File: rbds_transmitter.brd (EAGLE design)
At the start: 80 x 100 mm, 136 parts, among them J2 AVRISP-6, Q1 P-CH, Q2 P-Ch, Q3 P-Ch, T1 ATB3225-75032CT, T2 ATB3225-75032CT, U1 MAX2606, U2 TS974, U3 TS974, U4 MAX1551, U5 ATMEGA328, U6 TPS61030, U7 MCP4812, X1 16Mhz

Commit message: wiring up modules
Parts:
- moved ANT1 306.7 mm to (96.5, 119.4)
- moved C21 306.7 mm to (94.0, 114.3)
- moved C34 306.7 mm to (96.5, 114.3)
- moved C35 306.7 mm to (97.8, 101.0)
- moved C36 306.7 mm to (99.1, 105.4)
- moved C37 306.7 mm to (102.2, 105.4)
- moved L2 306.7 mm to (91.4, 105.4)
- moved R30 306.7 mm to (92.4, 110.5)
- moved R45 306.7 mm to (98.1, 110.5)
- moved TP8 306.7 mm to (92.7, 100.3)
- moved U1 306.7 mm to (95.2, 105.4)
- moved P1 302.8 mm to (129.5, 38.1), turned to 90 degrees
- moved B1 270.3 mm to (27.9, 21.6)
- moved J1 270.3 mm to (7.62, 21.6)
- moved L1 270.3 mm to (21.6, 38.1)
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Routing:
- net LCD5: track 0.00 -> 86.2 mm, vias 0 -> 2
- net LCD3: track 0.00 -> 84.2 mm, vias 0 -> 2
- net LCD2: track 0.00 -> 82.9 mm, vias 0 -> 2
- net LCD4: track 0.00 -> 80.5 mm
- net BPSK: track 5.10 -> 79.1 mm, vias 0 -> 1
- net LCD1: track 0.00 -> 63.4 mm, vias 0 -> 1
- net LCD0: track 0.00 -> 60.9 mm
- net AGND: track 36.7 -> 66.2 mm, vias 0 -> 2
- net CARRIER: track 0.00 -> 15.1 mm
- net ISP-MOSI: track 12.3 -> 0.00 mm
- net N$50: track 29.8 -> 20.7 mm
- net ISP-SCK: track 3.66 -> 12.7 mm
- net N$21: track 4.70 -> 7.50 mm
- net MOSI: track 0.00 -> 2.72 mm
- net SCK: track 0.00 -> 2.46 mm
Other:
- board size 80 x 100 mm -> 119.4 x 106.3 mm

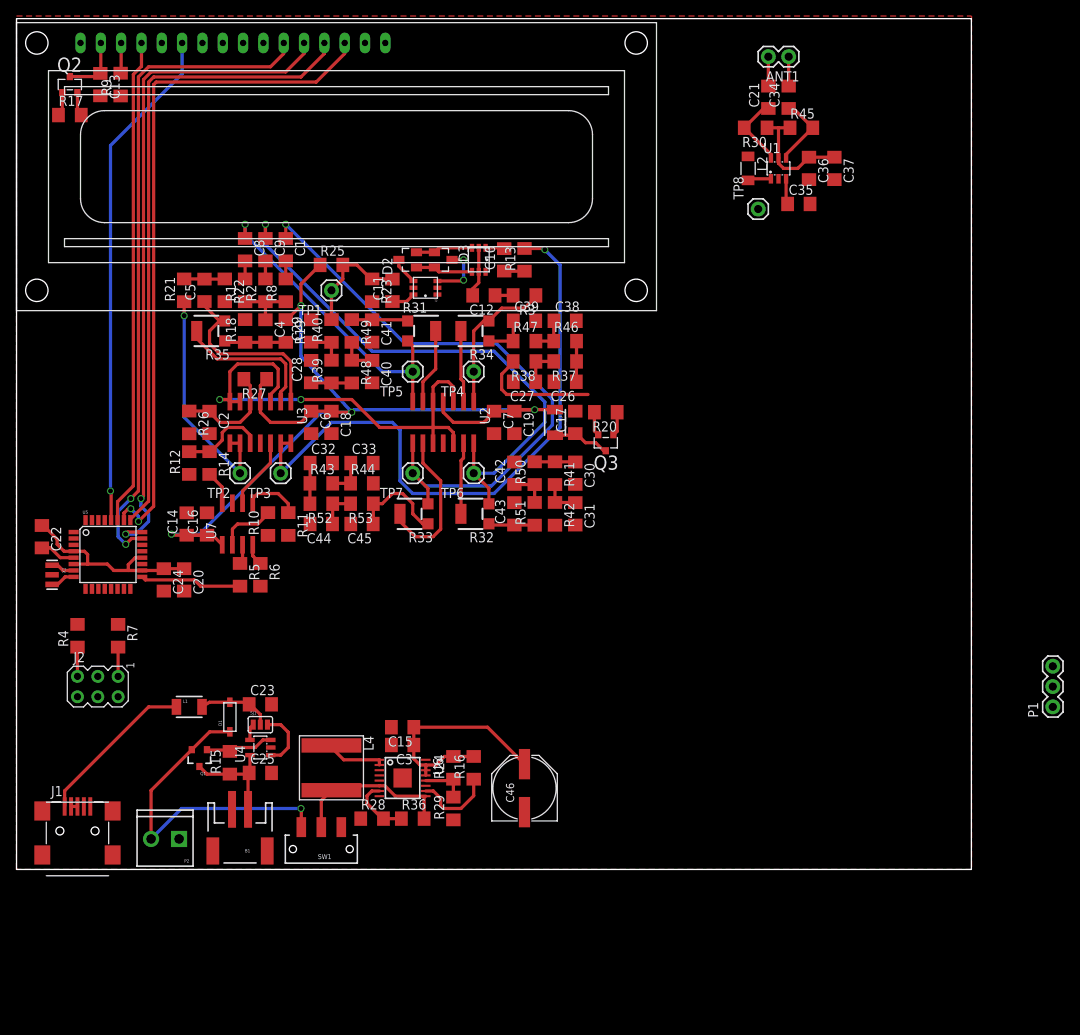
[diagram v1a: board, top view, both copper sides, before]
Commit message: changed mcu agnd to gnd: request engineering change form
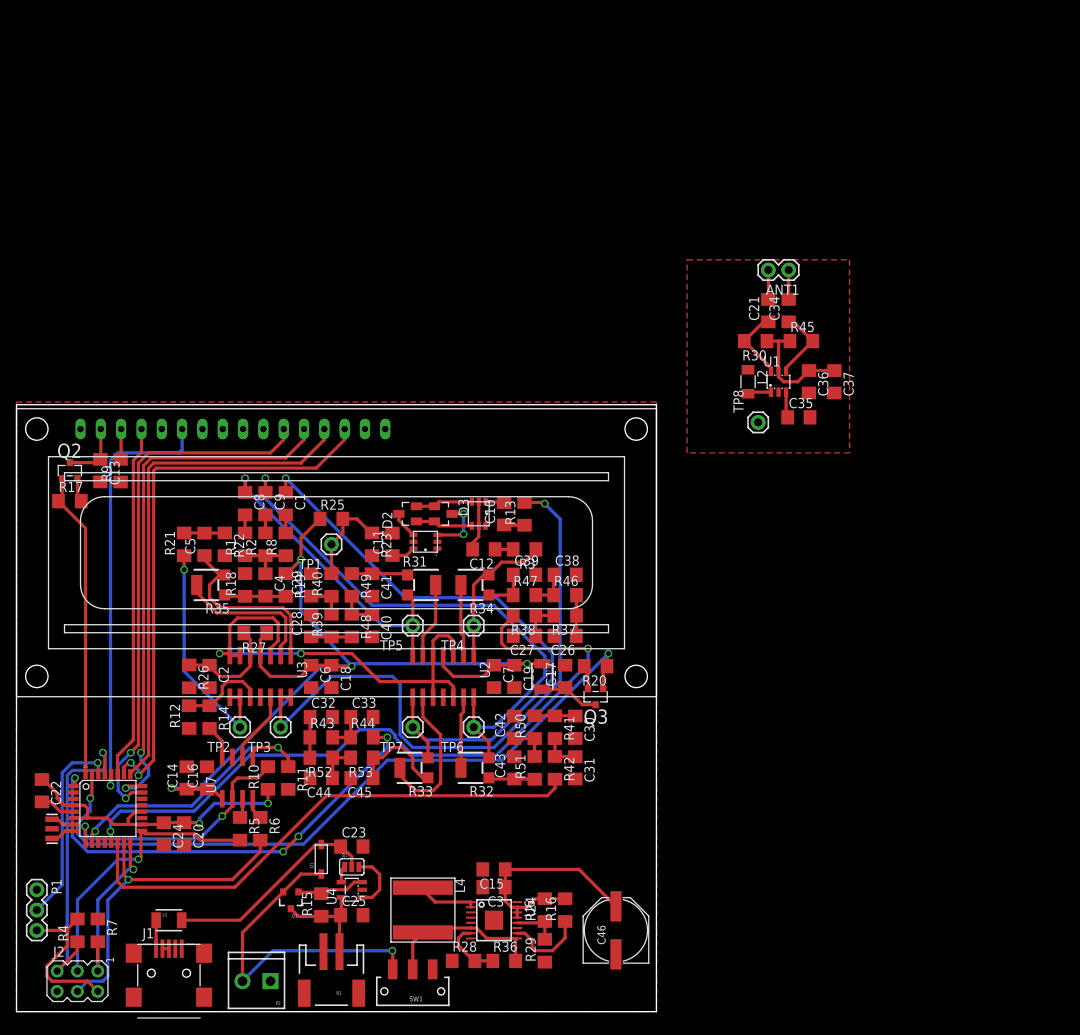
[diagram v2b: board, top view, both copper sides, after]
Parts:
- moved P1 129.0 mm to (2.54, 15.2), turned to 270 degrees
- moved C13 48.3 mm to (10.5, 67.6)
- moved Q2 48.3 mm to (6.67, 67.6)
- moved R9 48.3 mm to (13.0, 67.6)
- moved LCD1 48.3 mm to (0.00, 39.4)
- moved R17 48.3 mm to (6.67, 63.8)
- moved J2 36.9 mm to (7.62, 3.81)
- moved R7 36.9 mm to (10.2, 10.2)
- moved R4 36.8 mm to (7.62, 10.2)
- moved L3 31.8 mm to (65.7, 41.9)
- moved Q3 31.8 mm to (72.4, 39.4)
- moved R20 31.8 mm to (72.4, 43.2)
- moved C17 31.8 mm to (68.6, 41.9)
- moved C10 31.8 mm to (61.0, 62.2)
- moved C28 31.8 mm to (36.8, 48.3)
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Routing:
- net !TX_EN: track 3.03 -> 89.6 mm, vias 0 -> 2
- net CARRIER: track 15.1 -> 90.4 mm, vias 0 -> 2
- net PILOT: track 0.00 -> 66.1 mm
- net TONE: track 0.00 -> 57.1 mm, vias 0 -> 4
- net ISP-MOSI: track 0.00 -> 41.9 mm, vias 0 -> 1
- net !ISP-RST: track 3.81 -> 39.6 mm, vias 0 -> 1
- net !LCD_EN: track 3.09 -> 38.6 mm
- net +5V: track 61.1 -> 94.6 mm, vias 0 -> 2
- net !DAC_LATCH: track 6.93 -> 35.9 mm, vias 0 -> 2
- net RXD: track 0.00 -> 24.9 mm, vias 0 -> 1
- net !DAC_CS: track 7.35 -> 31.7 mm, vias 0 -> 2
- net ISP-SCK: track 12.7 -> 35.1 mm, vias 0 -> 1
- net ISP-MISO: track 3.66 -> 22.1 mm, vias 0 -> 1
- net N$1: track 9.81 -> 27.5 mm
- net N$54: track 20.6 -> 4.02 mm
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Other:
- board size 119.4 x 106.3 mm -> 80 x 75.9 mm

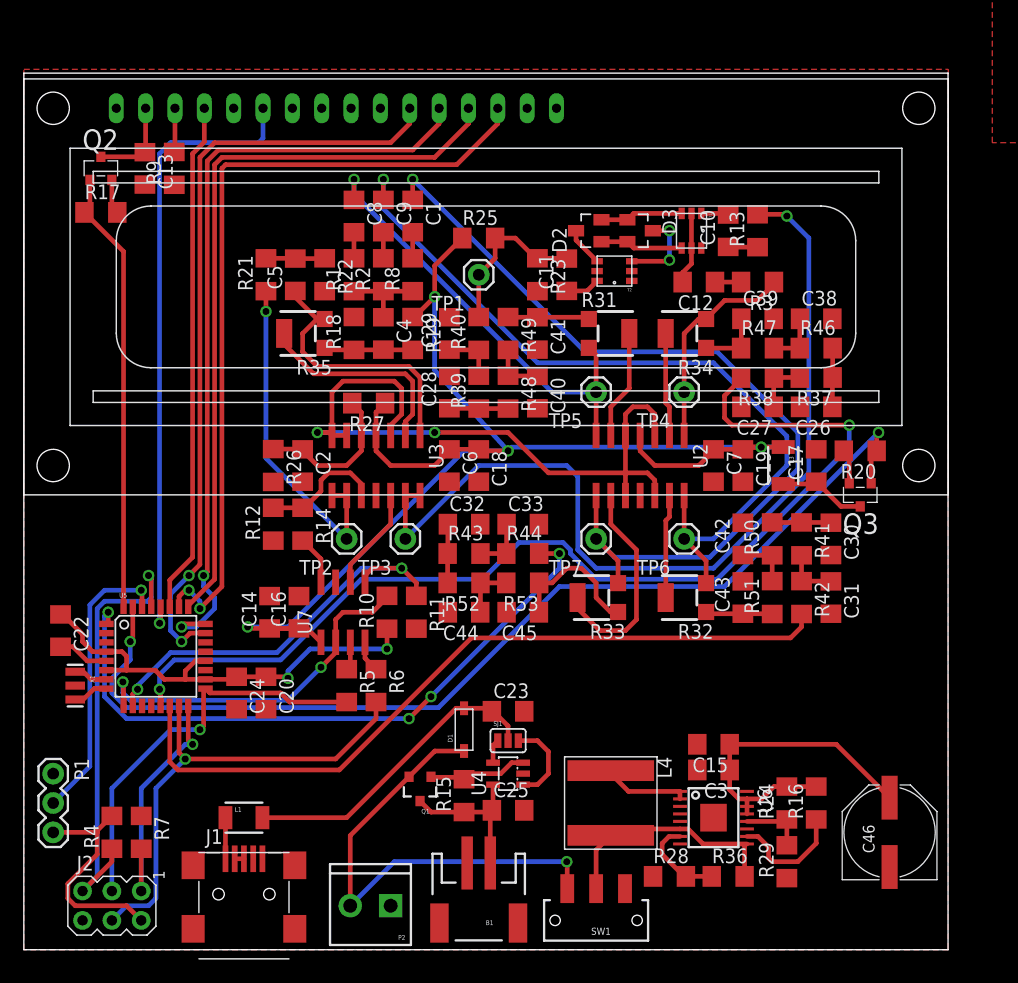
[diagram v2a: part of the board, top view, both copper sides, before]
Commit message: few more airwires
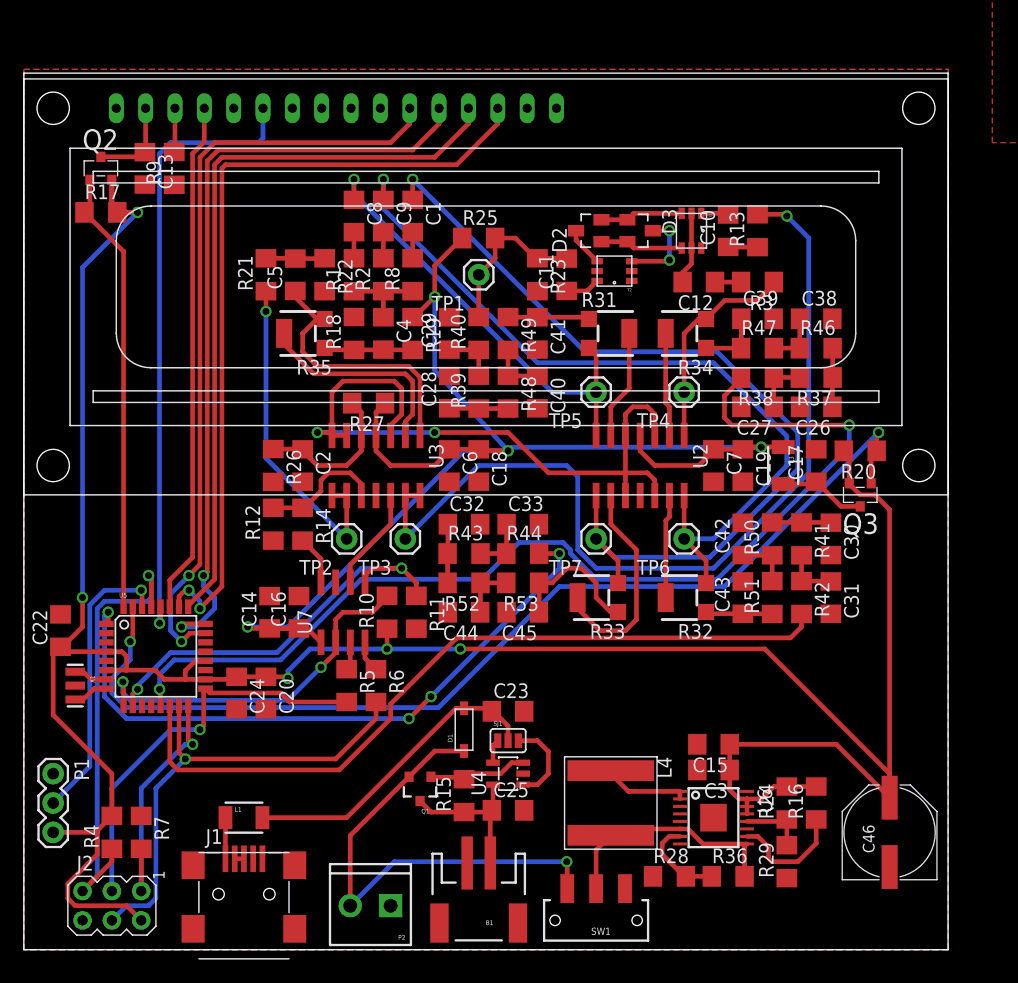
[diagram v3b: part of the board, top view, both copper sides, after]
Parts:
- turned C22 to 90 degrees
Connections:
- net AGND: no longer C22.2, U5.5
- net GND: now also C22.2, U5.5
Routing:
- net +5V: track 94.6 -> 232.7 mm, vias 2 -> 5
- net AGND: track 66.2 -> 61.8 mm
- net PILOT: track 66.1 -> 66.8 mm
- added copper zone on layer 16, net GND
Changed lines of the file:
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@@
 <element name="U5" library="sparkfun" package="TQFP32-08" value="ATMEGA328" x="11.43" y="25.4"/>
 <element name="C20" library="adafruit" package="C1206" value="4.7uF" x="20.955" y="22.225" rot="R270"/>
-<element name="C22" library="adafruit" package="C1206" value="0.1uF" x="3.175" y="27.6225" rot="R270"/>
+<element name="C22" library="adafruit" package="C1206" value="0.1uF" x="3.175" y="27.6225" rot="R90"/>
 <element name="J2" library="adafruit" package="AVRISP" value="AVRISP-6" x="7.62" y="3.81" rot="R270"/>
 <element name="LCD1" library="adafruit" package="LCD1602" value="HD44780LCD-1602" x="0" y="39.37"/>
@@
 <vertex x="83.82" y="69.85"/>
 </polygon>
-<wire x1="69.98" y1="54.61" x2="91.44" y2="80.24" width="0" layer="19" extent="1-1"/>
+<contactref element="U5" pad="5"/>
+<contactref element="C22" pad="2"/>
+<polygon width="0.4064" layer="16">
+<vertex x="0" y="0"/>
+<vertex x="0" y="76.2"/>
+<vertex x="80.01" y="76.2"/>
+<vertex x="80.01" y="0"/>
+</polygon>
+<wire x1="91.44" y1="80.24" x2="69.98" y2="54.61" width="0" layer="19" extent="1-1"/>
 </signal>
 <signal name="+5V">
@@
 <contactref element="C46" pad="+"/>
 <wire x1="61.09" y1="17.78" x2="61.09" y2="15.5575" width="0.4064" layer="1"/>
-<wire x1="74.93" y1="13.16" x2="70.31" y2="17.78" width="0.4064" layer="1"/>
-<wire x1="70.31" y1="17.78" x2="61.09" y2="17.78" width="0.4064" layer="1"/>
-<wire x1="7.1374" y1="25.8" x2="5.95" y2="25.8" width="0.4064" layer="1"/>
-<wire x1="5.95" y1="25.8" x2="5.08" y2="26.67" width="0.4064" layer="1"/>
-<wire x1="5.08" y1="27.305" x2="5.08" y2="26.67" width="0.4064" layer="1"/>
 <wire x1="20.955" y1="23.625" x2="18.415" y2="23.625" width="0.4064" layer="1"/>
 <wire x1="15.7226" y1="23.4" x2="18.19" y2="23.4" width="0.4064" layer="1"/>
@@
 <wire x1="31.4325" y1="27.788" x2="31.4325" y2="26.035" width="0.4064" layer="1"/>
 <via x="31.4325" y="26.035" extent="1-16" drill="0.6"/>
-<wire x1="3.175" y1="29.0225" x2="3.3625" y2="29.0225" width="0.4064" layer="1"/>
-<wire x1="3.3625" y1="29.0225" x2="5.08" y2="27.305" width="0.4064" layer="1"/>
 <wire x1="10.16" y1="2.54" x2="8.89" y2="3.81" width="0.4064" layer="1"/>
 <wire x1="8.89" y1="3.81" x2="4.445" y2="3.81" width="0.4064" layer="1"/>
@@
 <wire x1="6.35" y1="8.255" x2="6.35" y2="10.16" width="0.4064" layer="1"/>
 <wire x1="6.35" y1="10.312" x2="7.62" y2="11.582" width="0.4064" layer="1"/>
-<wire x1="71.44" y1="40.37" x2="71.44" y2="42.86" width="0.4064" layer="1"/>
-<wire x1="71.44" y1="42.86" x2="71.12" y2="43.18" width="0.4064" layer="1"/>
-<wire x1="70.968" y1="43.18" x2="71.12" y2="43.18" width="0.4064" layer="1"/>
 <wire x1="2.54" y1="10.16" x2="6.35" y2="10.16" width="0.4064" layer="1"/>
 <wire x1="6.35" y1="10.312" x2="6.35" y2="10.16" width="0.4064" layer="1"/>
-<wire x1="70.31" y1="17.78" x2="71.44" y2="40.37" width="0" layer="19" extent="1-1"/>
-<wire x1="31.4325" y1="26.035" x2="61.09" y2="17.78" width="0" layer="19" extent="1-1"/>
-<wire x1="7.62" y1="11.582" x2="7.1374" y2="24.2" width="0" layer="19" extent="1-1"/>
-<wire x1="8.0895" y1="63.8175" x2="3.3625" y2="29.0225" width="0" layer="19" extent="1-1"/>
+<wire x1="3.175" y1="26.2225" x2="3.5975" y2="25.8" width="0.4064" layer="1"/>
+<wire x1="3.5975" y1="25.8" x2="7.1374" y2="25.8" width="0.4064" layer="1"/>
+<wire x1="7.62" y1="11.582" x2="7.62" y2="15.24" width="0.4064" layer="1"/>
+<wire x1="7.62" y1="15.24" x2="2.54" y2="20.32" width="0.4064" layer="1"/>
+<wire x1="2.54" y1="20.32" x2="2.54" y2="25.5875" width="0.4064" layer="1"/>
+<wire x1="2.54" y1="25.5875" x2="3.175" y2="26.2225" width="0.4064" layer="1"/>
+<wire x1="8.0895" y1="63.8175" x2="7.62" y2="64.287" width="0.4064" layer="1"/>
+<wire x1="7.62" y1="64.287" x2="7.62" y2="66.675" width="0.4064" layer="1"/>
+<wire x1="3.175" y1="26.2225" x2="3.175" y2="26.3525" width="0.4064" layer="1"/>
+<wire x1="3.175" y1="26.3525" x2="3.4925" y2="26.3525" width="0.4064" layer="1"/>
+<wire x1="3.4925" y1="26.3525" x2="5.08" y2="27.94" width="0.4064" layer="1"/>
+<wire x1="5.08" y1="27.94" x2="5.08" y2="30.48" width="0.4064" layer="1"/>
+<via x="5.08" y="30.48" extent="1-16" drill="0.6"/>
+<wire x1="5.08" y1="30.48" x2="5.08" y2="59.055" width="0.4064" layer="16"/>
+<wire x1="5.08" y1="59.055" x2="9.8425" y2="63.8175" width="0.4064" layer="16"/>
+<via x="9.8425" y="63.8175" extent="1-16" drill="0.6"/>
+<wire x1="9.8425" y1="63.8175" x2="8.0895" y2="63.8175" width="0.4064" layer="1"/>
+<wire x1="74.93" y1="13.16" x2="70.31" y2="17.78" width="0.4064" layer="1"/>
+<wire x1="70.31" y1="17.78" x2="61.09" y2="17.78" width="0.4064" layer="1"/>
+<wire x1="71.44" y1="40.37" x2="71.44" y2="42.708" width="0.4064" layer="1"/>
+<wire x1="71.44" y1="42.708" x2="70.968" y2="43.18" width="0.4064" layer="1"/>
+<wire x1="71.44" y1="40.37" x2="71.44" y2="40.32" width="0.4064" layer="1"/>
+<wire x1="71.44" y1="40.32" x2="72.39" y2="39.37" width="0.4064" layer="1"/>
+<wire x1="72.39" y1="39.37" x2="73.66" y2="39.37" width="0.4064" layer="1"/>
+<wire x1="73.66" y1="39.37" x2="74.93" y2="38.1" width="0.4064" layer="1"/>
+<wire x1="74.93" y1="38.1" x2="74.93" y2="15.24" width="0.4064" layer="1"/>
+<wire x1="74.93" y1="15.24" x2="74.93" y2="13.16" width="0.4064" layer="1"/>
+<wire x1="31.4325" y1="26.035" x2="37.7825" y2="26.035" width="0.4064" layer="16"/>
+<via x="37.7825" y="26.035" extent="1-16" drill="0.6"/>
+<wire x1="37.7825" y1="26.035" x2="64.135" y2="26.035" width="0.4064" layer="1"/>
+<wire x1="64.135" y1="26.035" x2="74.93" y2="15.24" width="0.4064" layer="1"/>
 </signal>
 <signal name="ISP-MISO">
@@
 </signal>
 <signal name="AGND">
-<contactref element="U5" pad="5"/>
-<contactref element="C22" pad="2"/>
 <contactref element="U3" pad="6"/>
 <contactref element="U3" pad="7"/>
@@
 <wire x1="31.75" y1="45.4025" x2="32.7025" y2="46.355" width="0.4064" layer="1"/>
 <wire x1="26.67" y1="48.26" x2="26.67" y2="44.51" width="0.4064" layer="1"/>
-<wire x1="7.1374" y1="25" x2="5.48" y2="25" width="0.4064" layer="1"/>
-<wire x1="3.175" y1="26.2225" x2="4.2575" y2="26.2225" width="0.4064" layer="1"/>
-<wire x1="4.2575" y1="26.2225" x2="5.48" y2="25" width="0.4064" layer="1"/>
 <wire x1="32.7025" y1="46.355" x2="32.7025" y2="48.5775" width="0.4064" layer="1"/>
 <wire x1="32.7025" y1="48.5775" x2="32.0675" y2="49.2125" width="0.4064" layer="1"/>
@@
 <wire x1="25.4" y1="44.7675" x2="26.4125" y2="44.7675" width="0.4064" layer="1"/>
 <wire x1="26.4125" y1="44.7675" x2="26.67" y2="44.51" width="0.4064" layer="1"/>
-<wire x1="7.1374" y1="25" x2="25.4" y2="44.7675" width="0" layer="19" extent="1-16"/>
 </signal>
 <signal name="N$2">
@@
 <wire x1="12.63" y1="16.2625" x2="13.335" y2="15.5575" width="0.4064" layer="1"/>
 <wire x1="13.335" y1="15.5575" x2="27.305" y2="15.5575" width="0.4064" layer="1"/>
-<wire x1="38.735" y1="26.9875" x2="66.3575" y2="26.9875" width="0.4064" layer="1"/>
+<wire x1="37.465" y1="26.9875" x2="66.3575" y2="26.9875" width="0.4064" layer="1"/>
 <wire x1="66.3575" y1="26.9875" x2="67.31" y2="27.94" width="0.4064" layer="1"/>
 <wire x1="67.31" y1="27.94" x2="67.31" y2="29.058" width="0.4064" layer="1"/>
-<wire x1="38.735" y1="26.9875" x2="27.305" y2="15.5575" width="0.4064" layer="1"/>
+<wire x1="27.305" y1="15.5575" x2="31.75" y2="20.0025" width="0.4064" layer="1"/>
+<wire x1="31.75" y1="20.0025" x2="31.75" y2="21.2725" width="0.4064" layer="1"/>
+<wire x1="31.75" y1="21.2725" x2="37.465" y2="26.9875" width="0.4064" layer="1"/>
 </signal>
 <signal name="TONE">
